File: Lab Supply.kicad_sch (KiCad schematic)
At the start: 90 parts, among them J1 V-, J2 V+, M1 Fan_4pin, Q1 2N3904, Q2 2N3904, Q3 TIP121, Q4 BD139, SW1 ENABLE, U1 LM324, U2 LM7805_TO220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

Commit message: WIP
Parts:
- removed RV3, RV4: 100, symbol Device:R_Potentiometer
- removed V1, V3: 4.096, symbol Simulation_SPICE:VDC
- removed V2: 39, symbol Simulation_SPICE:VDC
- added H4: Control, Connector_PinHeader_2.54mm:PinHeader_1x04_P2.54mm_Vertical, symbol Headers:Control Header
- D1, D2: value SB140-E3/54 -> SB140; symbol Device:D -> Diode:SB140
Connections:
- net GND: now also H4.1 (GND), H4.3 (GND)
- net at U6.19 (D4): now also H4.2 (LOCK)
- net at U6.21 (D1): now also H4.4 (SET)
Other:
- moved on the sheet: C10, C11, C12, C15, C16, C5, C6, C7, C8, C9, D1, D2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

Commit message: First working version
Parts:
- removed C19: 100n, Capacitor_THT:C_Disc_D3.4mm_W2.1mm_P2.50mm, symbol Device:C
- R1: value 10k -> 15k
- R17: value 10k -> 5.6k
- R25: value 10k -> 4.7k
- R26: value 220 -> 22
- RV1: value 20k -> 10k
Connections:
- net GND: now also R29.1, R30.1; no longer R29.2, R30.2
- net at M1.4 (PWM): now also U6.18 (D6); no longer U6.17 (D8)
- net at Q1.2 (B), R17.1: now also R30.2; no longer R30.1
- net at Q2.2 (B), R25.2: now also R29.2; no longer R29.1
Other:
- moved on the sheet: D10, R29, R30

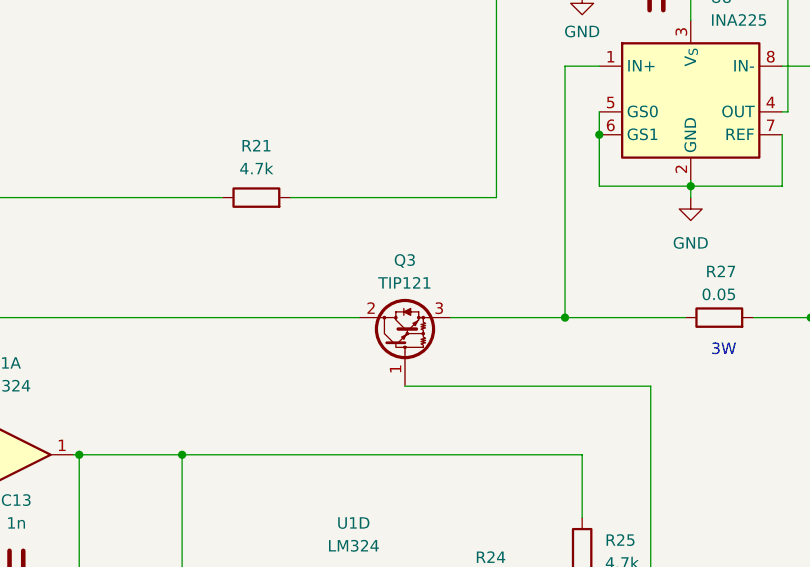
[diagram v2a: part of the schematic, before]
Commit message: Cleaned up documentation. Minor PCB changes
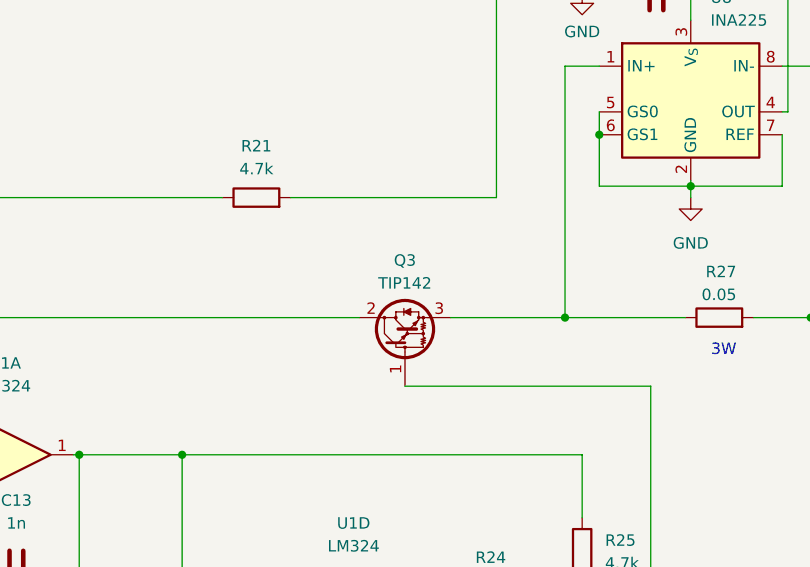
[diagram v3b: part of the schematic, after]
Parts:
- Q3: value TIP121 -> TIP142
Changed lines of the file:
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@@
       (effects (font (size 1.27 1.27)))
     )
-    (property "Value" "TIP121" (at 196.215 72.39 90)
+    (property "Value" "TIP142" (at 196.215 72.39 90)
       (effects (font (size 1.27 1.27)))
     )
